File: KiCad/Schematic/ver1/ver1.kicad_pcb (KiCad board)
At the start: 2 copper layers, 4 parts

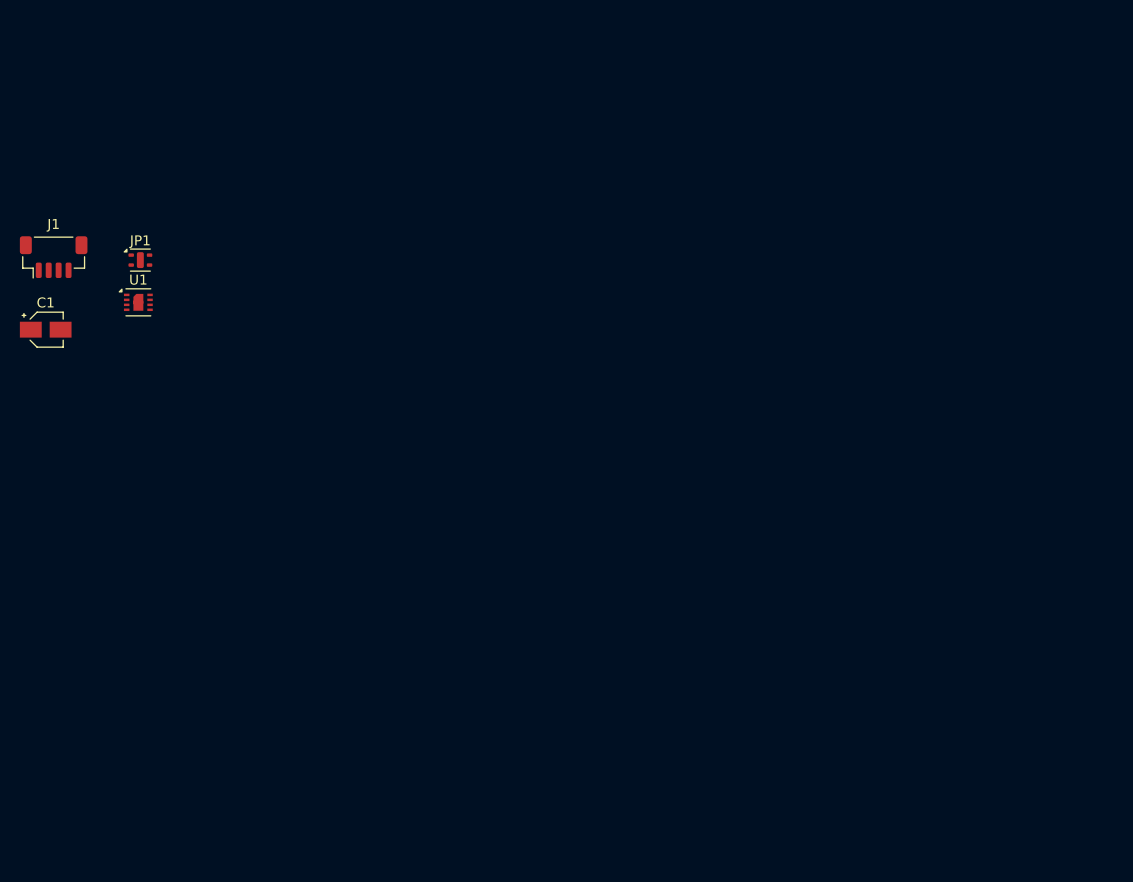
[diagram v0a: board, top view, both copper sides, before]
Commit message: Mild Setup for Arduino on VSCode + More Schematic
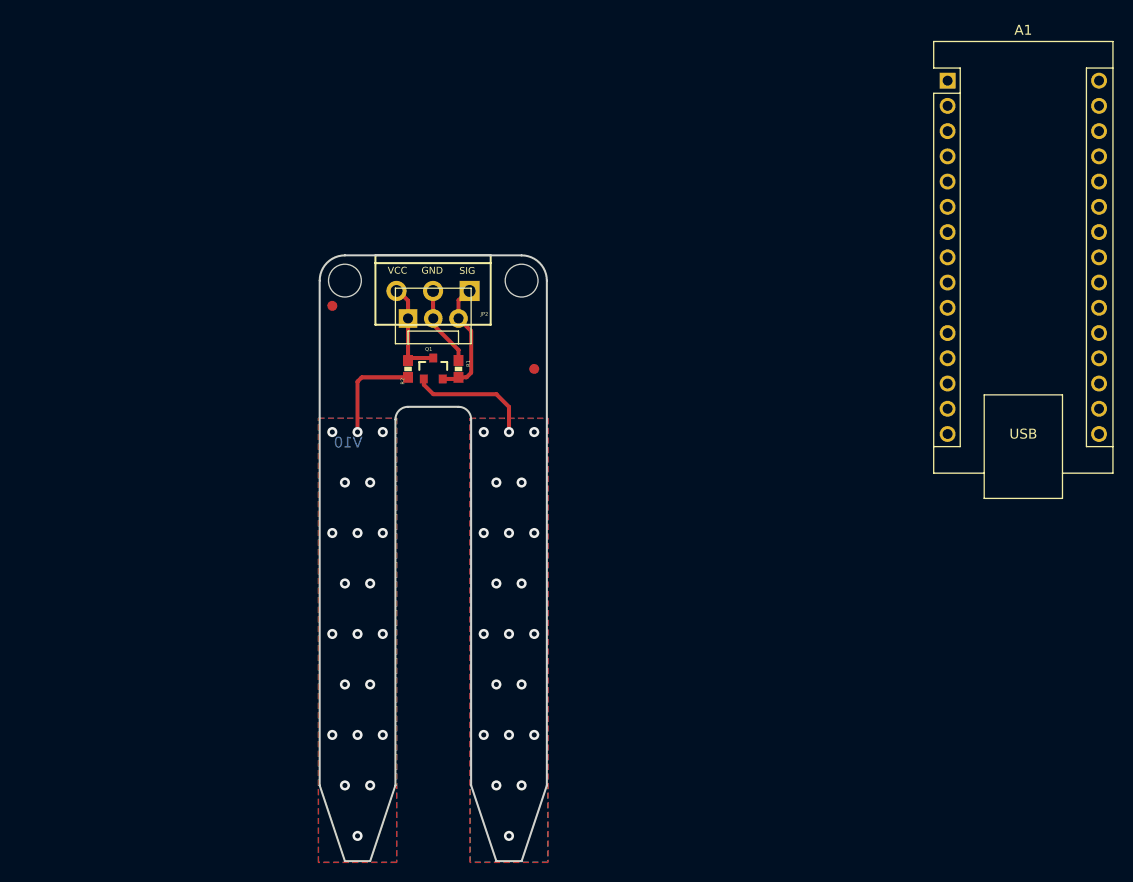
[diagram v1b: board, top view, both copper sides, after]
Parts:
- removed C1: ~, Capacitor_SMD:CP_Elec_3x5.3
- removed J1: ~, Connector_JST:JST_SH_BM04B-SRSS-TB_1x04-1MP_P1.00mm_Vertical
- removed U1: ~, Sensor_Humidity:Sensirion_DFN-8-1EP_2.5x2.5mm_P0.5mm_EP1.1x1.7mm
- added A1: Arduino_Nano_v2.x, Module:Arduino_Nano, F.Cu at (200.3, 56.9)
- added FID1: FIDUCIAL1X2, SparkFun_Soil_Moisture_Sensor:FIDUCIAL-1X2, F.Cu at (138.3, 79.6)
- added FID2: FIDUCIAL1X2, SparkFun_Soil_Moisture_Sensor:FIDUCIAL-1X2, F.Cu at (158.7, 86.0)
- added FRAME1: FRAME-LETTER, SparkFun_Soil_Moisture_Sensor:CREATIVE_COMMONS, F.Cu at (129.5, 145.6)
- added JP2: M03SCREW_LOCK, SparkFun_Soil_Moisture_Sensor:SCREWTERMINAL-3.5MM-3_LOCK.007S, F.Cu at (152.0, 78.1)
- added LOGO1: SFE_LOGO_NAME_FLAME.1_INCH, SparkFun_Soil_Moisture_Sensor:SFE_LOGO_NAME_FLAME_.1, B.Cu at (154.9, 87.2)
- added LOGO2: OSHW-LOGOS, SparkFun_Soil_Moisture_Sensor:OSHW-LOGO-S, B.Cu at (157.4, 80.9)
- added Q1: TRANSISTOR_NPNMMBT2222A, SparkFun_Soil_Moisture_Sensor:SOT23-3, F.Cu at (148.5, 86.0)
- added R1: 10k, SparkFun_Soil_Moisture_Sensor:0603-RES, F.Cu at (151.0, 86.0)
- added R2: 100, SparkFun_Soil_Moisture_Sensor:0603-RES, F.Cu at (146.0, 86.0)
- added STANDOFF1: STAND-OFF, SparkFun_Soil_Moisture_Sensor:STAND-OFF, F.Cu at (139.6, 77.1)
- added STANDOFF2: STAND-OFF, SparkFun_Soil_Moisture_Sensor:STAND-OFF, F.Cu at (157.4, 77.1)
- JP1: value ~ -> M03POLAR; footprint Sensor_Humidity:Sensirion_DFN-4-1EP_2x2mm_P1mm_EP0.7x1.6mm -> SparkFun_Soil_Moisture_Sensor:MOLEX-1X3
- moved JP1 27.6 mm to (146.0, 80.9)
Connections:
- JP1 pad 1: Net-(U1-~{(MISO})1) -> VCC
- JP1 pad 2: +3.3V -> GND
- JP1 pad 3: Net-(J1-SCL) -> /SIG
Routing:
- net /PROBE1: track 0.00 -> 12.6 mm, vias 0 -> 21
- net /SIG: track 0.00 -> 12.4 mm
- net /PROBE2: track 0.00 -> 10.3 mm, vias 0 -> 21
- net VCC: track 0.00 -> 10.2 mm
- net GND: track 0.00 -> 8.06 mm
- added copper zone on B.Cu, net /PROBE1
- added copper zone on F.Cu, net /PROBE1
- added copper zone on B.Cu, net /PROBE2
- added copper zone on F.Cu, net /PROBE2
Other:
- board outline added: 22.9 x 61 mm
- board text added: "GND"
- board text added: "Joel Bartlett"
- board text added: "SIG"
- board text added: "Soil Moisture Sensor"
- board text added: "V10"
- board text added: "VCC"
